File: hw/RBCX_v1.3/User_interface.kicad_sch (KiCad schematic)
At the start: 63 parts

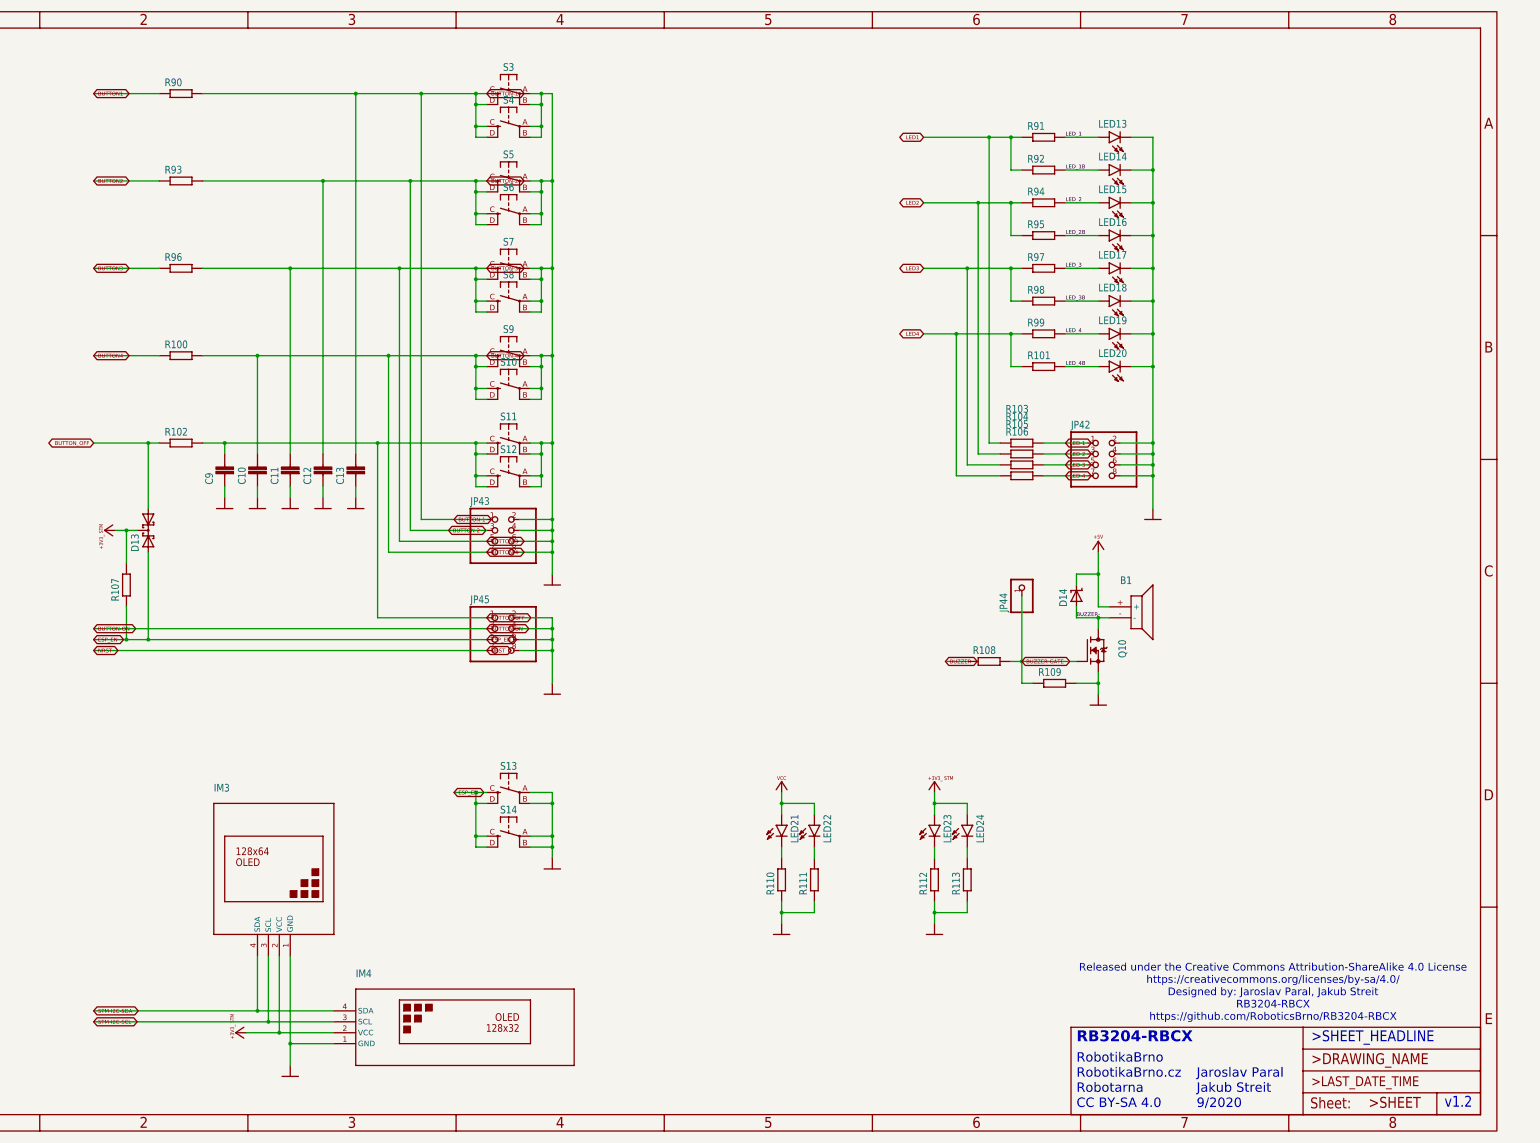
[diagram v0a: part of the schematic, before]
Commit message: Remove stepdowns, Micro-USB; fixup region names
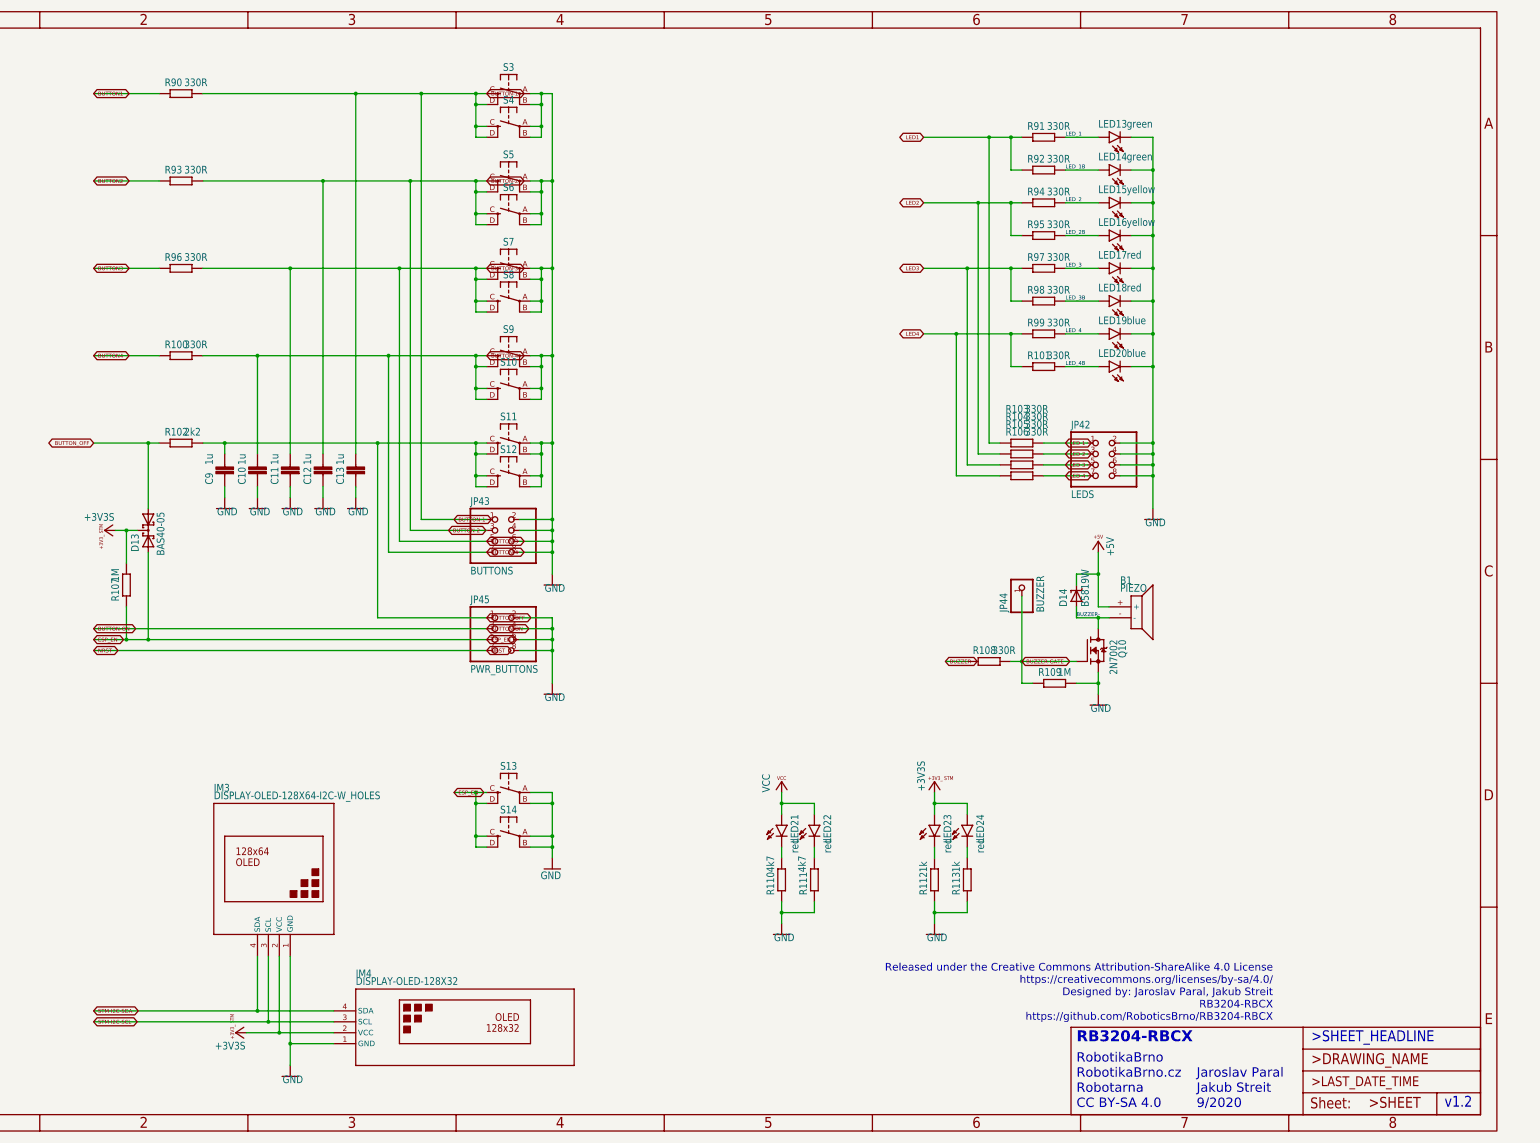
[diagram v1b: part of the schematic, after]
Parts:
- B1: value (none) -> PIEZO; footprint (none) -> RBCX:PIEZO
- C10, C11, C12, C13, C9: footprint (none) -> RBCX:C0402
- D13: value (none) -> BAS40-05; footprint (none) -> RBCX:SOT23
- D14: footprint (none) -> RBCX:SOD123
- IM3: value (none) -> DISPLAY-OLED-128X64-I2C-W_HOLES; footprint (none) -> RBCX:DISPLAY-OLED-128X64-I2C_W-HOLES
- IM4: value (none) -> DISPLAY-OLED-128X32; footprint (none) -> RBCX:DISPLAY-OLED-128X32
- JP42: value (none) -> LEDS; footprint (none) -> RBCX:2X04
- JP43: value (none) -> BUTTONS; footprint (none) -> RBCX:2X04
- JP44: value (none) -> BUZZER; footprint (none) -> RBCX:1X01
- JP45: value (none) -> PWR_BUTTONS; footprint (none) -> RBCX:2X04
- LED13, LED14: value (none) -> green; footprint (none) -> RBCX:CHIPLED_0603
- LED15, LED16: value (none) -> yellow; footprint (none) -> RBCX:CHIPLED_0603
- LED17, LED18, LED21, LED22, LED23, LED24: value (none) -> red; footprint (none) -> RBCX:CHIPLED_0603
- LED19, LED20: value (none) -> blue; footprint (none) -> RBCX:CHIPLED_0603
- Q10: footprint (none) -> RBCX:SOT23
- R100, R101, R103, R104, R105, R106, R108, R90, R91, R92, R93, R94, R95, R96, R97, R98, R99: value (none) -> 330R; footprint (none) -> RBCX:R0402
- R102: value (none) -> 2k2; footprint (none) -> RBCX:R0402
- R107, R109: value (none) -> 1M; footprint (none) -> RBCX:R0402
- R110, R111: value (none) -> 4k7; footprint (none) -> RBCX:R0402
- R112, R113: value (none) -> 1k; footprint (none) -> RBCX:R0402
- S10, S11, S12, S13, S14, S3, S4, S5, S6, S7, S8, S9: value (none) -> TS-1187A-C-C-B; footprint (none) -> RBCX:TS-1187A

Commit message: Everything everywhere all et once
Conversion to a new look
-  splitting the whole diagram for better orientation on multiple sheets using Kicad functions. Division of the whole schematics within several hierarchical sheets without globally named trac, using only wires, local labels and hierarchical labels.

Add new features
- Battery charger with cell balancer (With whole battery measurement)
- USB PD Sink Controller

Change old features
-  removing many 5V stepdowns and replacing them with only one strong stepdown (continuous 8A, peak 12A)
-  New power switcher design to connect VUSB to the VCC power line when no battery is connected.
(The reason for the new design is the implementation of Power deliveri => high voltage capability on VUSB 5-12V).

Remove micro_USB
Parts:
- removed B1: PIEZO, RBCX:PIEZO, symbol RBCX-eagle-import:PIEZO
- removed C10, C11, C12, C13, C9: (no value), RBCX:C0402, symbol RBCX-eagle-import:C-EUC0402
- removed D13: BAS40-05, RBCX:SOT23, symbol RBCX-eagle-import:BAS40-05
- removed D14: (no value), RBCX:SOD123, symbol RBCX-eagle-import:SHOTTKY-SOD123
- removed IM3: DISPLAY-OLED-128X64-I2C-W_HOLES, RBCX:DISPLAY-OLED-128X64-I2C_W-HOLES, symbol RBCX-eagle-import:DISPLAY-OLED-128X64-I2C-W_HOLES
- removed IM4: DISPLAY-OLED-128X32, RBCX:DISPLAY-OLED-128X32, symbol RBCX-eagle-import:DISPLAY-OLED-128X32
- removed JP42: LEDS, RBCX:2X04, symbol RBCX-eagle-import:PINHD-2X4
- removed JP43: BUTTONS, RBCX:2X04, symbol RBCX-eagle-import:PINHD-2X4
- removed JP44: BUZZER, RBCX:1X01, symbol RBCX-eagle-import:PINHD-1X1
- removed JP45: PWR_BUTTONS, RBCX:2X04, symbol RBCX-eagle-import:PINHD-2X4
- removed LED13, LED14: green, RBCX:CHIPLED_0603, symbol RBCX-eagle-import:LEDCHIPLED_0603
- removed LED15, LED16: yellow, RBCX:CHIPLED_0603, symbol RBCX-eagle-import:LEDCHIPLED_0603
- removed LED17, LED18, LED21, LED22, LED23, LED24: red, RBCX:CHIPLED_0603, symbol RBCX-eagle-import:LEDCHIPLED_0603
- removed LED19, LED20: blue, RBCX:CHIPLED_0603, symbol RBCX-eagle-import:LEDCHIPLED_0603
- removed Q10: (no value), RBCX:SOT23, symbol RBCX-eagle-import:N-MOSFET-SOT23-GSD
- removed R100, R101, R103, R104, R105, R106, R108, R90, R91, R92, R93, R94, R95, R96, R97, R98, R99: 330R, RBCX:R0402, symbol RBCX-eagle-import:R-EU_R0402
- removed R102: 2k2, RBCX:R0402, symbol RBCX-eagle-import:R-EU_R0402
- removed R107, R109: 1M, RBCX:R0402, symbol RBCX-eagle-import:R-EU_R0402
- removed R110, R111: 4k7, RBCX:R0402, symbol RBCX-eagle-import:R-EU_R0402
- removed R112, R113: 1k, RBCX:R0402, symbol RBCX-eagle-import:R-EU_R0402
- removed S10, S11, S12, S13, S14, S3, S4, S5, S6, S7, S8, S9: TS-1187A-C-C-B, RBCX:TS-1187A, symbol RBCX-eagle-import:10-XX_SMD
- added B?: PIEZO, RBCX:PIEZO, symbol RBCX-eagle-import:PIEZO
- added C? (x5): 1uF, Resistor_SMD:R_0402_1005Metric, symbol Device:C
- added D?: D, Diode_SMD:D_SOD-523, symbol Device:D
- added IM?: DISPLAY-OLED-128X32, RBCX:DISPLAY-OLED-128X32, symbol RBCX-eagle-import:DISPLAY-OLED-128X32
- added IM?: DISPLAY-OLED-128X64-I2C-W_HOLES, RBCX:DISPLAY-OLED-128X64-I2C-W_HOLES, symbol RBCX-eagle-import:DISPLAY-OLED-128X64-I2C-W_HOLES
- added J?: Conn_01x01, Connector_PinSocket_2.54mm:PinSocket_1x01_P2.54mm_Vertical, symbol Connector_Generic:Conn_01x01
- added J? (x3): Conn_02x04_Counter_Clockwise, Connector_PinHeader_2.54mm:PinHeader_2x04_P2.54mm_Vertical, symbol Connector_Generic:Conn_02x04_Counter_Clockwise
- added J?: Conn_01x02, Connector_PinHeader_2.54mm:PinHeader_1x02_P2.54mm_Vertical, symbol Connector_Generic:Conn_01x02
- added LED? (x2): blue, LED_SMD:LED_0603_1608Metric, symbol RBCX-eagle-import:LEDCHIPLED_0603
- added LED? (x2): red, LED_SMD:LED_0603_1608Metric, symbol RBCX-eagle-import:LEDCHIPLED_0603
- added LED? (x2): green, LED_SMD:LED_0603_1608Metric, symbol RBCX-eagle-import:LEDCHIPLED_0603
- added LED? (x2): yellow, LED_SMD:LED_0603_1608Metric, symbol RBCX-eagle-import:LEDCHIPLED_0603
- added Q? (x2): Q_NMOS_DGS, Package_TO_SOT_SMD:SOT-723, symbol Device:Q_NMOS_DGS
- added R? (x19): 330, Capacitor_SMD:C_0201_0603Metric, symbol Device:R
- added R? (x2): 1M, Resistor_SMD:R_0201_0603Metric, symbol Device:R
- added R?: 2.2k, Resistor_SMD:R_0201_0603Metric, symbol Device:R
- added R?: 100k, Capacitor_SMD:C_0201_0603Metric, symbol Device:R
- added SW? (x12): SW, Button_Switch_SMD:SW_Push_1P1T_NO_CK_KSC6xxJ, symbol RBCX:SW
- added TP?: TP_06MM, RBCX:TP_06MM, symbol RBCX-eagle-import:TP_06MM
- added U?: BAT54C, Package_TO_SOT_SMD:SOT-23, symbol RBCX:BAT54C
- added X? (x30): 52559-3092, RBCX:52559-3092, symbol RBCX-eagle-import:52559-3092
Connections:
- net BUTTON-1: now also C?.1, J?.1 (Pin_1), R?.2, SW?.1 (P1), SW?.1 (P1), X?.18 (S)
- net BUTTON-2: now also C?.1, J?.2 (Pin_2), R?.2, SW?.1 (P1), SW?.1 (P1), X?.19 (S)
- net BUTTON-3: now also C?.1, J?.3 (Pin_3), R?.2, R?.2, SW?.1 (P1), SW?.1 (P1), X?.20 (S)
- net BUTTON-4: now also C?.1, J?.4 (Pin_4), R?.2, SW?.1 (P1), SW?.1 (P1), X?.21 (S)
- net BUTTON-OFF: now also C?.1, J?.1 (Pin_1), R?.2, SW?.1 (P1), SW?.1 (P1), X?.17 (S)
- net BUTTON-ON: now also J?.2 (Pin_2), X?.16 (S)
- net BUTTON1: now also R?.1
- net BUTTON2: now also R?.1
- net BUTTON3: now also R?.1
- net BUTTON4: now also R?.1
- net BUTTON_OFF: now also R?.1, U?.2 (A2)
- net BUZZER: now also R?.1
- net BUZZER-: now also B?.-, D?.2 (A), Q?.1 (D)
- net BUZZER-GATE: now also J?.1 (Pin_1), Q?.2 (G), R?.1, R?.2, X?.3 (S)
- net ESP_EN: now also J?.3 (Pin_3), R?.1, R?.2, R?.2, SW?.1 (P1), SW?.1 (P1), U?.1 (A1), X?.15 (S)
- net GND: now also C?.2, C?.2, C?.2, C?.2, C?.2, IM?.1 (GND), IM?.1 (GND), J?.5 (Pin_5), J?.5 (Pin_5), J?.5 (Pin_5), J?.6 (Pin_6), J?.6 (Pin_6), J?.6 (Pin_6), J?.7 (Pin_7), J?.7 (Pin_7), J?.7 (Pin_7), J?.8 (Pin_8), J?.8 (Pin_8), J?.8 (Pin_8), LED?.C, LED?.C, LED?.C, LED?.C, LED?.C, LED?.C, LED?.C, LED?.C, Q?.3 (S), Q?.3 (S), R?.1, R?.2, SW?.2 (S1), SW?.2 (S1), SW?.2 (S1), SW?.2 (S1), SW?.2 (S1), SW?.2 (S1), SW?.2 (S1), SW?.2 (S1), SW?.2 (S1), SW?.2 (S1), SW?.2 (S1), SW?.2 (S1), X?.22 (S), X?.23 (S)
- net LED-1: now also J?.1 (Pin_1), R?.2, X?.7 (S)
- net LED-2: now also J?.2 (Pin_2), R?.2, X?.8 (S)
- net LED-3: now also J?.3 (Pin_3), R?.2, X?.9 (S)
- net LED-4: now also J?.4 (Pin_4), R?.2, X?.10 (S)
- net LED1: now also R?.1, R?.1, R?.1
- net LED2: now also R?.1, R?.1, R?.1
- net LED3: now also R?.1, R?.1, R?.1
- net LED4: now also R?.1, R?.1, R?.1
- net LED_1: now also LED?.A, R?.2
- net LED_1B: now also LED?.A, R?.2
- net LED_2: now also LED?.A, R?.2
- net LED_2B: now also LED?.A, R?.2
- net LED_3: now also LED?.A, R?.2
- net LED_3B: now also LED?.A, R?.2
- net LED_4: now also LED?.A, R?.2
- net LED_4B: now also LED?.A, R?.2
- net NRST: now also J?.4 (Pin_4), X?.14 (S)
- net STM-I2C-SCL: now also IM?.3 (SCL), IM?.3 (SCL), X?.25 (S)
- net STM-I2C-SDA: now also IM?.4 (SDA), IM?.4 (SDA), X?.24 (S)
- net VCC: now also X?.1 (S), X?.2 (S)
- new net: Q?.1 (D), R?.1
- new net 3V3: IM?.2 (VCC), IM?.2 (VCC), J?.1 (Pin_1), R?.1, U?.3 (C), X?.11 (S), X?.12 (S)
- new net 5V: B?.+, D?.1 (K), X?.5 (S), X?.6 (S)
- new net BOOT0: J?.2 (Pin_2), Q?.2 (G), R?.2, TP?.P$1 (TP), X?.13 (S)
- new net GPIO-2: X?.26 (S)
- new net ILED-5V: X?.4 (S)
- new net USB_DM: X?.28 (S)
- new net USB_DP: X?.27 (S)
- new net VUSB: X?.29 (S), X?.30 (S)
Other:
- note added: "BOOT1"
- note added: "UI BOARD"
- note added: "v1.3"
- note removed: "v1.2"

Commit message: Work in progress
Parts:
- removed J? (x3): Conn_02x04_Counter_Clockwise, Connector_PinHeader_2.54mm:PinHeader_2x04_P2.54mm_Vertical, symbol Connector_Generic:Conn_02x04_Counter_Clockwise
- removed LED? (x2): blue, LED_SMD:LED_0603_1608Metric, symbol RBCX-eagle-import:LEDCHIPLED_0603
- removed LED? (x2): red, LED_SMD:LED_0603_1608Metric, symbol RBCX-eagle-import:LEDCHIPLED_0603
- removed LED? (x2): green, LED_SMD:LED_0603_1608Metric, symbol RBCX-eagle-import:LEDCHIPLED_0603
- removed LED? (x2): yellow, LED_SMD:LED_0603_1608Metric, symbol RBCX-eagle-import:LEDCHIPLED_0603
- added D33, D34: green, LED_SMD:LED_0603_1608Metric, symbol Device:LED
- added D35, D36: yellow, LED_SMD:LED_0603_1608Metric, symbol Device:LED
- added D37, D38: red, LED_SMD:LED_0603_1608Metric, symbol Device:LED
- added D39, D40: blue, LED_SMD:LED_0603_1608Metric, symbol Device:LED
- added J30, J31, J33: Conn_02x04_Odd_Even, Connector_PinHeader_2.54mm:PinHeader_2x04_P2.54mm_Vertical, symbol Connector_Generic:Conn_02x04_Odd_Even
- SW1, SW10, SW11, SW12, SW2, SW3, SW4, SW5, SW6, SW7, SW8, SW9: renamed from SW?; footprint Button_Switch_SMD:SW_Push_1P1T_NO_CK_KSC6xxJ -> RBCX:SW
- U3: renamed from U?; footprint Package_TO_SOT_SMD:SOT-23 -> Package_TO_SOT_SMD:SOT-323_SC-70; LCSC C2762215 -> C57891
- gave numbers to parts that had none: 38
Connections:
- net BUTTON-1: now also J31.1 (Pin_1)
- net BUTTON-2: now also J31.3 (Pin_3)
- net BUTTON-3: now also J31.5 (Pin_5)
- net BUTTON-4: now also J31.7 (Pin_7)
- net BUTTON-OFF: now also J33.1 (Pin_1)
- net BUTTON-ON: now also J33.3 (Pin_3)
- net ESP_EN: no longer R78.2
- net GND: now also D33.1 (K), D34.1 (K), D35.1 (K), D36.1 (K), D37.1 (K), D38.1 (K), D39.1 (K), D40.1 (K), J30.2 (Pin_2), J30.4 (Pin_4), J30.6 (Pin_6), J30.8 (Pin_8), J31.2 (Pin_2), J31.4 (Pin_4), J31.6 (Pin_6), J31.8 (Pin_8), J33.2 (Pin_2), J33.4 (Pin_4), J33.6 (Pin_6), J33.8 (Pin_8)
- net LED-1: now also J30.1 (Pin_1)
- net LED-2: now also J30.3 (Pin_3)
- net LED-3: now also J30.5 (Pin_5)
- net LED-4: now also J30.7 (Pin_7)
- net LED_1: now also D33.2 (A)
- net LED_1B: now also D34.2 (A)
- net LED_2: now also D35.2 (A)
- net LED_2B: now also D36.2 (A)
- net LED_3: now also D37.2 (A)
- net LED_3B: now also D38.2 (A)
- net LED_4: now also D39.2 (A)
- net LED_4B: now also D40.2 (A)
- net NRST: now also J33.7 (Pin_7)
- new net ESP-EN: J33.5 (Pin_5), R78.2

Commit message: New PCB layout
some changes of schema:
- change PD sink AO33772 to AO33771
- remove power switch
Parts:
- J30, J31, J33: footprint Connector_PinHeader_2.54mm:PinHeader_2x04_P2.54mm_Vertical -> RBCX:PinHeader_2x04_P2.54mm_Vertical
- J32: footprint Connector_PinHeader_2.54mm:PinHeader_1x02_P2.54mm_Vertical -> RBCX:PinHeader_1x02_P2.54mm_Vertical
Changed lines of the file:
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@@
     (property "Reference" "J33" (id 0) (at 208.28 135.89 0))
     (property "Value" "Conn_02x04_Odd_Even" (id 1) (at 208.28 138.43 0))
-    (property "Footprint" "Connector_PinHeader_2.54mm:PinHeader_2x04_P2.54mm_Vertical" (id 2) (at 207.01 144.78 0)
+    (property "Footprint" "RBCX:PinHeader_2x04_P2.54mm_Vertical" (id 2) (at 207.01 144.78 0)
       (effects (font (size 1.27 1.27)) hide)
     )
@@
     (property "Reference" "J31" (id 0) (at 208.28 118.11 0))
     (property "Value" "Conn_02x04_Odd_Even" (id 1) (at 208.28 120.65 0))
-    (property "Footprint" "Connector_PinHeader_2.54mm:PinHeader_2x04_P2.54mm_Vertical" (id 2) (at 207.01 127 0)
+    (property "Footprint" "RBCX:PinHeader_2x04_P2.54mm_Vertical" (id 2) (at 207.01 127 0)
       (effects (font (size 1.27 1.27)) hide)
     )
@@
     (property "Reference" "J30" (id 0) (at 71.12 88.9 0))
     (property "Value" "Conn_02x04_Odd_Even" (id 1) (at 71.12 91.44 0))
-    (property "Footprint" "Connector_PinHeader_2.54mm:PinHeader_2x04_P2.54mm_Vertical" (id 2) (at 69.85 97.79 0)
+    (property "Footprint" "RBCX:PinHeader_2x04_P2.54mm_Vertical" (id 2) (at 69.85 97.79 0)
       (effects (font (size 1.27 1.27)) hide)
     )
@@
       (effects (font (size 1.27 1.27)) (justify left))
     )
-    (property "Footprint" "Connector_PinHeader_2.54mm:PinHeader_1x02_P2.54mm_Vertical" (id 2) (at 269.24 127 0)
-      (effects (font (size 1.27 1.27)) hide)
-    )
+    (property "Footprint" "RBCX:PinHeader_1x02_P2.54mm_Vertical" (id 2) (at 269.24 127 0)
+      (effects (font (size 1.27 1.27)) hide)
+    )
